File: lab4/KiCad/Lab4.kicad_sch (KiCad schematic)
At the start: 0 parts

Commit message: Integrate Lab 4 MCU support, diagnostics and hierarchical connections
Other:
- sheet Cockpit zone ports: added +3V3, +5V, CAN_A_H, CAN_A_L, CAN_B_H, CAN_B_L, GND; removed none
- sheet Front zone ports: added +3V3, +6V6_SERVO, CAN_A_H, CAN_A_L, CAN_B_H, CAN_B_L, GND; removed none
- sheet Power ports: added +3V3, +5V, +6V6_SERVO, GND; removed none
- sheet Rear zone ports: added +3V3, +5V, CAN_A_H, CAN_A_L, CAN_B_H, CAN_B_L, GND; removed none
- note added: "CAN_A_H/L and CAN_B_H/L are separate root nets. Same-name local labels on this root join the shown sheet pins. Child labels connect only through those ports. Power flags document external battery power and outputs after passive filters; they do not prove current capacity, regulation, thermal behavior or PCB completeness. See Verification.txt and Design-review.csv for current checks and open decis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"
- note added: "Front and rear are the terminated ends. Cockpit taps both backbones. Each zone has its own two isolation groups; termination remains on the bus side. Actuator connectors / motor protection / physical layout remain unfinished."
- note added: "LAB 4 - CONNECTIVITY OVERVIEW"
- note removed: "Proposed circuits: six CAN front ends, three analog current sensors and three buck converters. Open: bare-MCU/actuator integration, final protection and power validation, hierarchy, layout. Local labels do not connect across sheets; finish hierarchy before board import. See Design-review.csv and the shared Lab 4 Writeup for decisions and unresolved checks."
- company: (none) -> Team 4
- title: Lab 4 - Three-zone PCB -> Lab 4 - three-zone controller

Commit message: Update Lab 4 circuits, assembly BOMs and measured PCB placement
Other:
- sheet Front zone ports: added +5V; removed none
- sheet Power ports: added VBAT_PROTECTED; removed none
- sheet Rear zone ports: added VBAT_PROTECTED; removed none

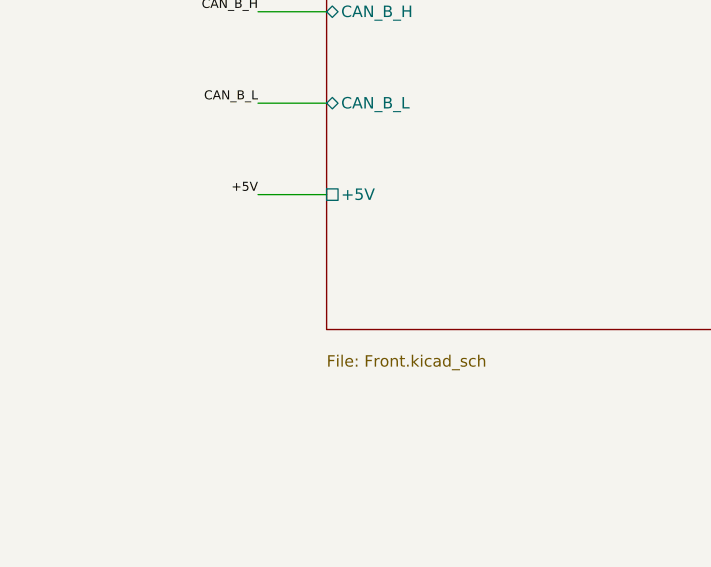
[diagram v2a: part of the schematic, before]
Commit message: Select approved LiPo pair and add battery voltage monitor
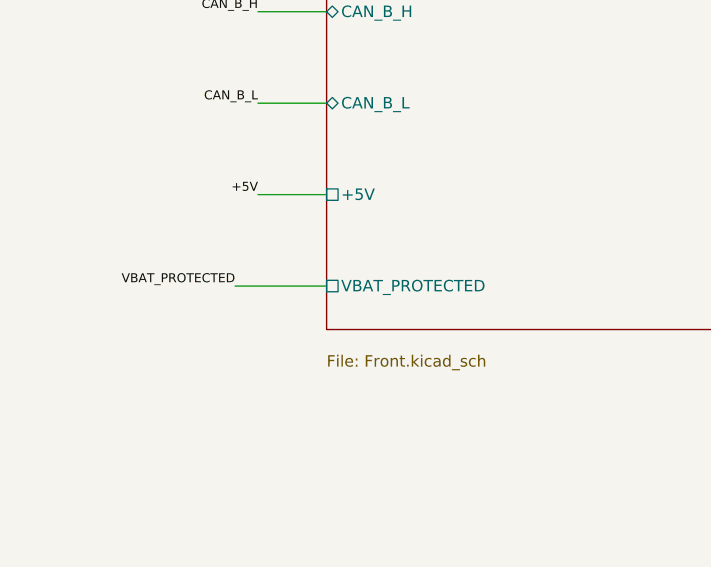
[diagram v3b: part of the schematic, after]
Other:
- sheet Front zone ports: added VBAT_PROTECTED; removed none
